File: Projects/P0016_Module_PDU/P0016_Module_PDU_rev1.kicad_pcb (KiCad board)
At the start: 2 copper layers, 100 parts, among them IC1 ATMEGA328P-A, J1 22-03-5045, J10 22-03-5045, J2 22-03-5045, J3 22-03-5045, J4 MULTICOMP_24.243.1, J5 MULTICOMP_24.243.2, J6 70543-0036, J7 70543-0036, J8 22-03-5045, J9 22-03-5045, P1 USB_OTG, P2 USB_OTG, P3 ICSP_02X03, Q1 NTD20N03L27, U1 MIC29302AWU-TR, U10 SN65176BDR, U11 SN65176BDR, U12 FT231XQ, U2 MIC29302AWU-TR, U3 MIC29302AWU-TR, U4 UA78M05CDCYR, U5 MIC29302AWU-TR, U6 MIC29302AWU-TR, U7 MIC29302AWU-TR, U8 LT6100CDD#PBF, U9 FT231XQ, Y1 ABM8-16.000MHZ-10-1-U-T

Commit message: Almost done placement for P0016
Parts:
- C13, C14, C15, C16, C17, C18, C19, C20, C21, C22, C4, C5, C9, L1, R1, R10, R11, R12, R13, R14, R15, R16, R17, R18, R19, R2, R20, R21, R22, R23, R24, R25, R26, R27, R28, R29, R3, R30, R31, R32, R33, R34, R35, R36, R4, R5, R6, R7, R8, R9: moved to B.Cu
- J10, J9: value 22-03-5045 -> 70543-0036; footprint Pin_Headers:Pin_Header_Straight_1x04 -> Pin_Headers:Pin_Header_Straight_1x02
- J4: value MULTICOMP_24.243.1 -> 22-03-5045; footprint open_robotics:MULTICOMP_4MM_JACK -> Pin_Headers:Pin_Header_Straight_1x04
- J5: value MULTICOMP_24.243.2 -> 22-03-5045; footprint open_robotics:MULTICOMP_4MM_JACK -> Pin_Headers:Pin_Header_Straight_1x04
- J6: value 70543-0036 -> 22-03-5045; footprint Pin_Headers:Pin_Header_Straight_1x02 -> Pin_Headers:Pin_Header_Straight_1x04
- J7: value 70543-0036 -> MULTICOMP_24.243.1; footprint Pin_Headers:Pin_Header_Straight_1x02 -> open_robotics:MULTICOMP_4MM_JACK
- J8: value 22-03-5045 -> MULTICOMP_24.243.2; footprint Pin_Headers:Pin_Header_Straight_1x04 -> open_robotics:MULTICOMP_4MM_JACK
- moved J4 131.3 mm to (166.4, 72.4)
- moved J5 128.3 mm to (166.4, 67.3)
- moved D11 127.8 mm to (152.4, 59.7)
- moved P3 126.8 mm to (155.7, 76.2), turned to 180 degrees
- moved C9 126.7 mm to (167.6, 92.7), turned to 270 degrees
- moved Q1 125.8 mm to (157.5, 121.9), turned to 180 degrees
- moved R35 122.3 mm to (157.5, 59.7), turned to 180 degrees
- moved U8 115.1 mm to (168.2, 89.3), turned to 90 degrees
- moved P1 114.4 mm to (139.5, 61.0)
- moved C14 111.6 mm to (147.3, 55.9)
- moved C13 110.4 mm to (147.3, 53.3)
- moved R16 110.2 mm to (144.8, 62.2), turned to 180 degrees
- moved R15 109.2 mm to (144.8, 59.7), turned to 180 degrees
- moved U9 108.7 mm to (147.3, 54.6), turned to 270 degrees
- moved C1 108.1 mm to (165.1, 128.3), turned to 90 degrees
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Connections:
- J10 pad 1: GND -> Net-(J10-Pad1)
- J10 pad 2: Net-(C12-Pad1) -> Net-(J10-Pad2)
- J2 pad 2: Net-(C2-Pad1) -> Net-(C10-Pad1)
- J3 pad 2: Net-(C3-Pad1) -> Net-(C2-Pad1)
- J4 pad 1: /VIN -> GND
- J5 pad 1: Net-(J5-Pad1) -> GND
- J6 pad 1: Net-(J6-Pad1) -> GND
- J6 pad 2: Net-(J6-Pad2) -> Net-(C12-Pad1)
- J7 pad 1: Net-(J6-Pad1) -> /VIN
- J8 pad 1: GND -> Net-(J8-Pad1)
- J9 pad 1: GND -> Net-(J10-Pad1)
- J9 pad 2: Net-(C11-Pad1) -> Net-(J10-Pad2)
- Q1 pad 2: Net-(J6-Pad2) -> Net-(J10-Pad2)
- Q1 pad 3: Net-(J5-Pad1) -> Net-(J8-Pad1)
- R7 pad 1: Net-(J6-Pad2) -> Net-(J10-Pad2)
- R7 pad 2: Net-(J5-Pad1) -> Net-(J8-Pad1)
- S1 pad 6: Net-(J6-Pad1) -> Net-(J10-Pad1)
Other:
- board outline added: 66 x 83.8 mm

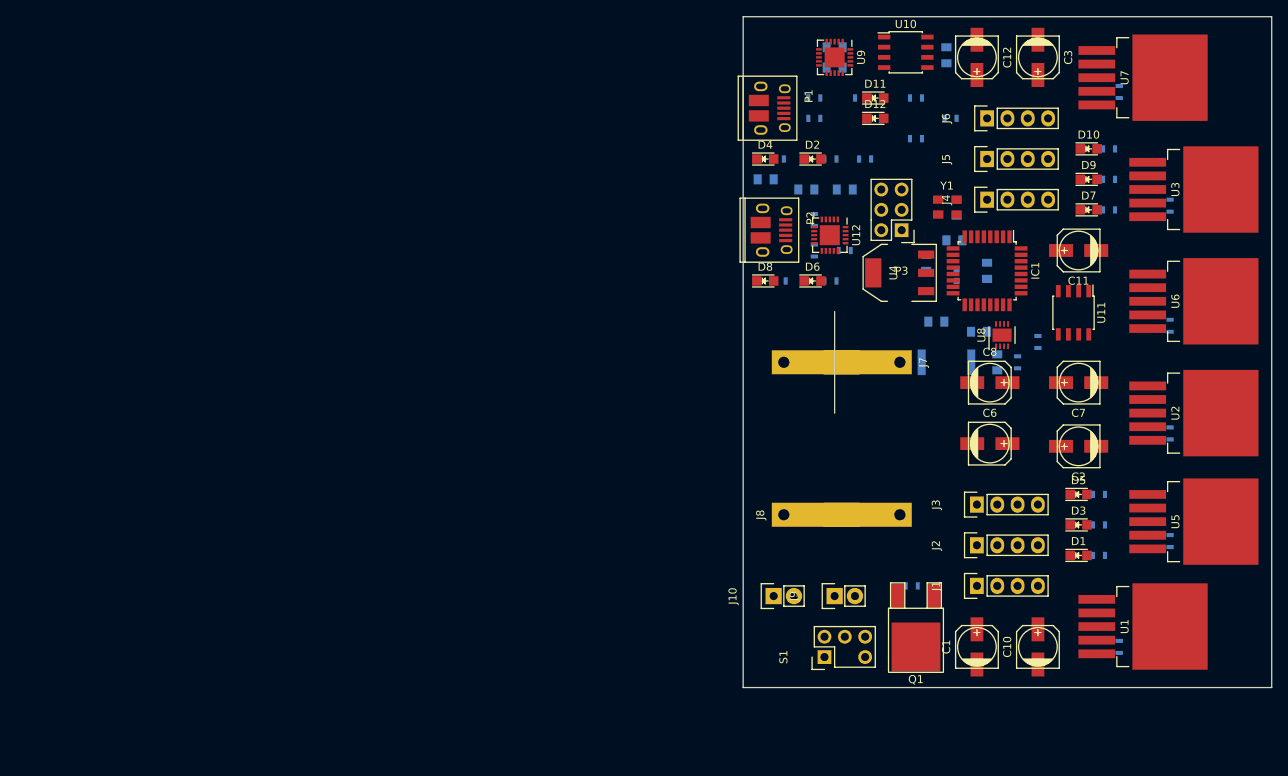
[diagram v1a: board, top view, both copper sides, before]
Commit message: Created RS485 to TTL adapter
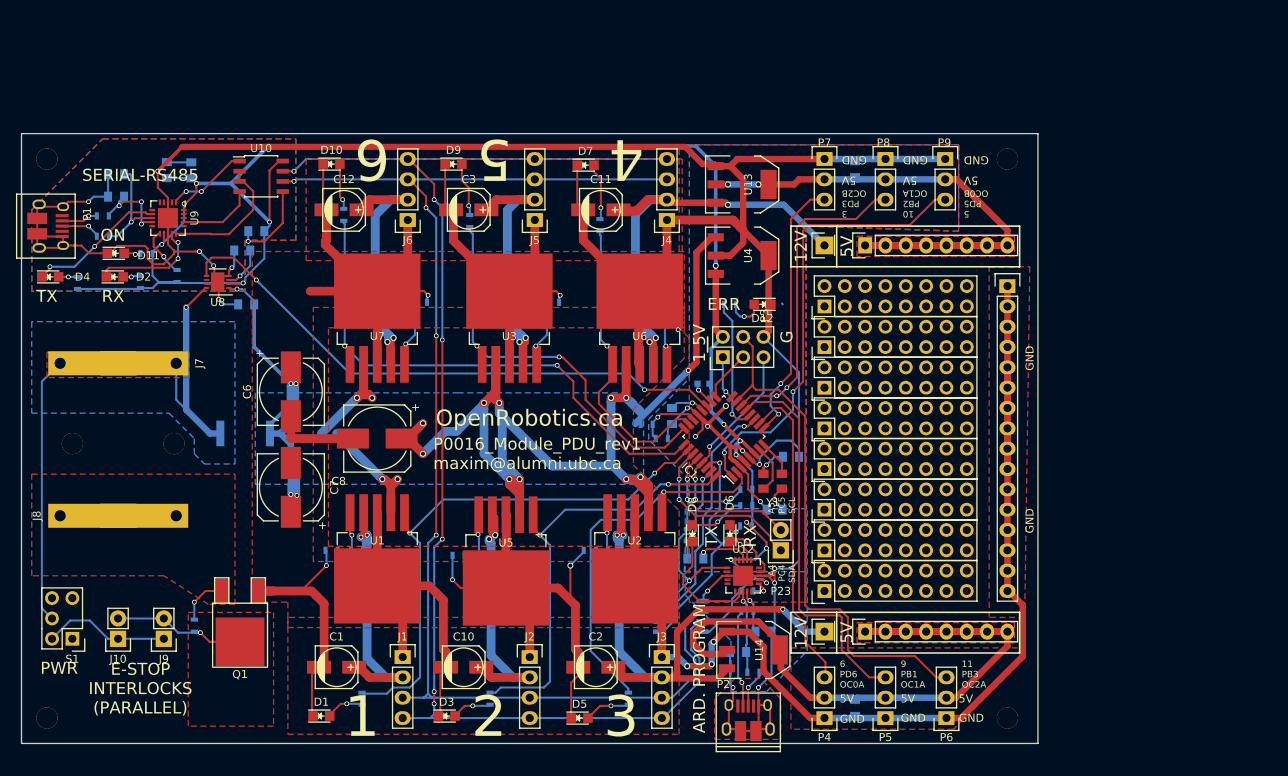
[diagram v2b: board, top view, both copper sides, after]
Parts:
- added C23: 0.1uF, Capacitors_SMD:C_0805, B.Cu at (149.9, 68.6)
- added C24: 0.1uF, Capacitors_SMD:C_0805, B.Cu at (149.9, 135.9)
- added P10: CONN_01X08, Pin_Headers:Pin_Header_Straight_1x08, F.Cu at (151.1, 126.4)
- added P11: CONN_02X08, Pin_Headers:Pin_Header_Straight_2x08, F.Cu at (146.1, 121.3)
- added P12: CONN_02X08, Pin_Headers:Pin_Header_Straight_2x08, F.Cu at (146.1, 116.2)
- added P13: CONN_02X08, Pin_Headers:Pin_Header_Straight_2x08, F.Cu at (146.1, 111.1)
- added P14: CONN_02X08, Pin_Headers:Pin_Header_Straight_2x08, F.Cu at (146.1, 106.0)
- added P15: CONN_01X16, Pin_Headers:Pin_Header_Straight_1x16, F.Cu at (168.9, 83.2)
- added P16: CONN_02X08, Pin_Headers:Pin_Header_Straight_2x08, F.Cu at (146.1, 101.0)
- added P17: CONN_02X08, Pin_Headers:Pin_Header_Straight_2x08, F.Cu at (146.1, 95.9)
- added P18: CONN_02X08, Pin_Headers:Pin_Header_Straight_2x08, F.Cu at (146.1, 90.8)
- added P19: CONN_02X08, Pin_Headers:Pin_Header_Straight_2x08, F.Cu at (146.1, 85.7)
- added P20: CONN_01X08, Pin_Headers:Pin_Header_Straight_1x08, F.Cu at (151.1, 78.1)
- added P21: CONN_01X01, Pin_Headers:Pin_Header_Straight_1x01, F.Cu at (146.1, 126.4)
- added P22: CONN_01X01, Pin_Headers:Pin_Header_Straight_1x01, F.Cu at (146.1, 78.1)
- added P23: CONN_01X02, Pin_Headers:Pin_Header_Straight_1x02, F.Cu at (140.6, 116.2)
- added P4: CONN_01X03, Pin_Headers:Pin_Header_Straight_1x03, F.Cu at (146.1, 137.2)
- added P5: CONN_01X03, Pin_Headers:Pin_Header_Straight_1x03, F.Cu at (153.7, 137.2)
- added P6: CONN_01X03, Pin_Headers:Pin_Header_Straight_1x03, F.Cu at (161.3, 137.2)
- added P7: CONN_01X03, Pin_Headers:Pin_Header_Straight_1x03, F.Cu at (146.1, 67.3)
- added P8: CONN_01X03, Pin_Headers:Pin_Header_Straight_1x03, F.Cu at (153.7, 67.3)
- added P9: CONN_01X03, Pin_Headers:Pin_Header_Straight_1x03, F.Cu at (161.1, 67.3)
- added U13: NCP1117ST50T3GOSCT, TO_SOT_Packages_SMD:SOT-223, F.Cu at (135.8, 70.5)
- added U14: NCP1117ST50T3GOSCT, TO_SOT_Packages_SMD:SOT-223, F.Cu at (137.2, 128.7)
- added X1: OP_HOLE, open_robotics:modular8_mounting_hole, F.Cu at (48.9, 137.2)
- added X2: OP_HOLE, open_robotics:modular8_mounting_hole, F.Cu at (168.9, 137.2)
- added X3: OP_HOLE, open_robotics:modular8_mounting_hole, F.Cu at (168.9, 67.3)
- added X4: OP_HOLE, open_robotics:modular8_mounting_hole, F.Cu at (48.9, 67.3)
- added X5: OP_HOLE, open_robotics:modular8_mounting_hole, F.Cu at (52.1, 102.9)
- added X6: OP_HOLE, open_robotics:modular8_mounting_hole, F.Cu at (64.8, 102.9)
- C6, C7, C8: footprint Capacitors_SMD:c_elec_5x4.5 -> Capacitors_SMD:c_elec_8x6.5
- U11: moved to B.Cu
- moved C22 103.3 mm to (63.9, 68.7), turned to 90 degrees
- moved R1 102.9 mm to (84.5, 116.2), turned to 0 degrees
- moved C7 99.3 mm to (79.4, 108.3), turned to 90 degrees
- moved U8 98.2 mm to (70.2, 82.7), turned to 180 degrees
- moved R35 98.1 mm to (61.3, 79.1)
- moved D11 96.9 mm to (57.5, 79.1)
- moved U7 96.8 mm to (90.2, 93.0), turned to 90 degrees
- moved D1 96.7 mm to (83.2, 136.9)
- moved R4 96.0 mm to (87.6, 116.2), turned to 0 degrees
- moved R34 96.0 mm to (86.0, 74.3), turned to 90 degrees
- moved R11 95.8 mm to (90.8, 85.2), turned to 180 degrees
- moved C17 95.5 mm to (66.9, 68.7), turned to 90 degrees
- moved C9 95.4 mm to (73.3, 78.7), turned to 180 degrees
- moved R14 94.7 mm to (95.6, 85.2), turned to 180 degrees
- moved D10 94.6 mm to (84.5, 67.9)
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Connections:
- net /MOSI renamed /11/PB3/OC2A
- net Net-(C11-Pad1) renamed /V4_12V
- net Net-(C2-Pad1) renamed /V3_12V
- IC1 pad 1: /EN2 -> /3/PD3/OC2B
- IC1 pad 10: /EN5 -> /6/PD6/OC0A
- IC1 pad 11: /EN6 -> /TXDEN_uC
- IC1 pad 13: (no net) -> /9/PB1/OC1A
- IC1 pad 14: /TXDEN_uC -> /10/PB2/OC1B
- IC1 pad 23: (no net) -> /EN4
- IC1 pad 24: (no net) -> /EN5
- IC1 pad 25: (no net) -> /EN6
- IC1 pad 26: (no net) -> /EN1
- IC1 pad 27: (no net) -> /SDA
- IC1 pad 28: (no net) -> /SCL
- IC1 pad 32: /EN1 -> /EN2
- IC1 pad 9: /EN4 -> /5/PD5/OC0B
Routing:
- net GND: track 0.00 -> 840.8 mm, vias 0 -> 28
- net /VBATT: track 0.00 -> 227.4 mm, vias 0 -> 20
- net /5V: track 0.00 -> 225.7 mm, vias 0 -> 13
- net /RS485-: track 0.00 -> 171.5 mm, vias 0 -> 6
- net /RS485+: track 0.00 -> 165.1 mm, vias 0 -> 4
- net /5V_POW_LEFT: track 0.00 -> 92.3 mm
- net /5V_POW_RIGHT: track 0.00 -> 77.0 mm, vias 0 -> 2
- net /EN1: track 0.00 -> 72.7 mm, vias 0 -> 2
- net /V3_12V: track 0.00 -> 72.1 mm, vias 0 -> 3
- net /I_SENSE: track 0.00 -> 72.1 mm, vias 0 -> 2
- net /EN6: track 0.00 -> 67.8 mm, vias 0 -> 2
- net /11/PB3/OC2A: track 0.00 -> 65.0 mm
- net /V4_12V: track 0.00 -> 64.4 mm, vias 0 -> 3
- net /VIN: track 0.00 -> 61.5 mm, vias 0 -> 1
- net /3/PD3/OC2B: track 0.00 -> 56.6 mm, vias 0 -> 2
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- added copper zone on F.Cu, net /5V_POW_LEFT
- added copper zone on F.Cu, net /5V_POW_RIGHT
- added copper zone on B.Cu, net /VBATT
- added copper zone on B.Cu, net /VIN
- added copper zone on F.Cu, net /VIN
- added copper zone on B.Cu, net GND
- added copper zone on F.Cu, net GND
- added copper zone on F.Cu, net Net-(J10-Pad2)
- added copper zone on F.Cu, net Net-(J8-Pad1)
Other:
- board size 66 x 83.8 mm -> 127 x 76.2 mm
- net class POW2A added: clearance 0.2, trace_width 2, via_dia 1, via_drill 0.6
- board text added: "1"
- board text added: "10 PB2 OC1A"
- board text added: "11 PB3 OC2A"
- board text added: "12V"
- board text added: "2"
- board text added: "3"
- board text added: "3 PD3 OC2B"
- board text added: "4"
- board text added: "5"
- board text added: "5 PD5 OC0B"
- board text added: "5V"
- board text added: "6"
- board text added: "6 PD6 OC0A"
- board text added: "9 PB1 OC1A"
- board text added: "A4 PC4 SDA"
- board text added: "A5 PC5 SCL"
- board text added: "ARD. PROGRAM"
- board text added: "E-STOP INTERLOCKS (PARALLEL)"
- board text added: "ERR"
- board text added: "G"
- board text added: "GND"
- board text added: "ON"
- board text added: "OpenRobotics.ca"
- board text added: "P0016_Module_PDU_rev1 maxim@alumni.ubc.ca"
- board text added: "PWR"
- board text added: "RX"
- board text added: "SERIAL-RS485"
- board text added: "TX"
